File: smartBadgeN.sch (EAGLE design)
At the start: 62 parts, among them IC1 SI1304BDL, J1 10118192-0001LF, J2 LiPo, J3 505278-2433, Q1 MBT3904DW1T1, Q2 2.5A/30V, U1 CP2102N, U2 AP2112K-3.3V, U3 ESP-WROOM-32, U4 MCP73831

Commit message: revB init
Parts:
- C3: value 0.1uF -> 10uF
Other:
- note added: "Rev B"
- note removed: "Rev A"
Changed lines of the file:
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@@
 <parts>
 <part name="R9" library="resistor" library_urn="urn:adsk.eagle:library:348" deviceset="R-EU_" device="R0603" package3d_urn="urn:adsk.eagle:package:23555/3" value="1k"/>
-<part name="C3" library="resistor" library_urn="urn:adsk.eagle:library:348" deviceset="C-EU" device="C0603" package3d_urn="urn:adsk.eagle:package:23616/2" value="0.1uF"/>
+<part name="C3" library="resistor" library_urn="urn:adsk.eagle:library:348" deviceset="C-EU" device="C0603" package3d_urn="urn:adsk.eagle:package:23616/2" value="10uF"/>
 <part name="GND11" library="supply1" library_urn="urn:adsk.eagle:library:371" deviceset="GND" device=""/>
 <part name="C5" library="resistor" library_urn="urn:adsk.eagle:library:348" deviceset="C-EU" device="C1206" package3d_urn="urn:adsk.eagle:package:23618/2" value="100uF"/>
@@
 <text x="284.48" y="7.62" size="1.778" layer="94" align="bottom-right">Desgin by Moritz von Stietencron @ IoT-FabLab | www.iotfablab.eu | info@iotfablab.eu
 c/o BIBA - Bremer Institut für Produktion und Logistik GmbH | Hochschulring 20 | 28359 Bremen | GERMANY</text>
-<text x="378.46" y="7.62" size="1.778" layer="94" align="top-center">Rev A</text>
+<text x="378.46" y="7.62" size="1.778" layer="94" align="top-center">Rev B</text>
 <wire x1="289.56" y1="111.76" x2="289.56" y2="27.94" width="0.1524" layer="97"/>
 <text x="292.1" y="109.22" size="2.54" layer="97">Test Pads</text>

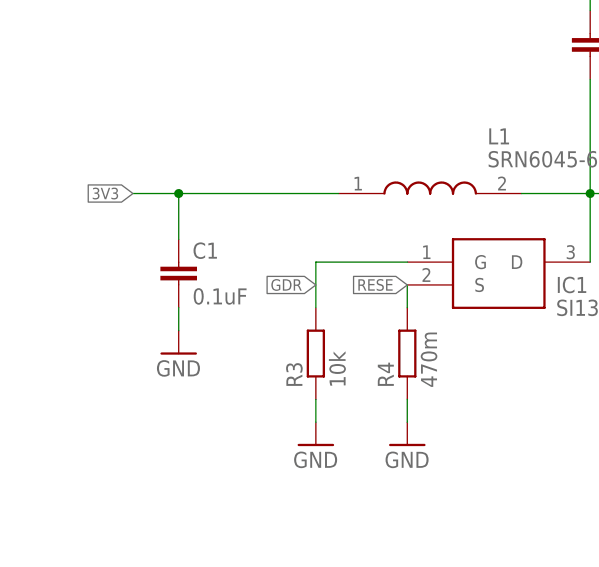
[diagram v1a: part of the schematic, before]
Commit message: capacitor values updated
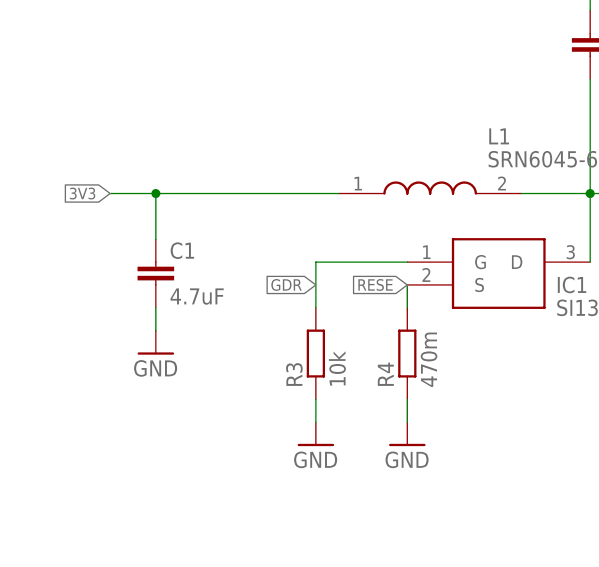
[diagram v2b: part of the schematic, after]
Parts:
- C1: value 0.1uF -> 4.7uF
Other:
- moved on the sheet: C1
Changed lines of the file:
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@@
 <part name="GND8" library="supply1" library_urn="urn:adsk.eagle:library:371" deviceset="GND" device=""/>
 <part name="L1" library="SamacSys_Parts" deviceset="SRN6045-680M" device=""/>
-<part name="C1" library="resistor" library_urn="urn:adsk.eagle:library:348" deviceset="C-EU" device="C0603" package3d_urn="urn:adsk.eagle:package:23616/2" value="0.1uF"/>
+<part name="C1" library="resistor" library_urn="urn:adsk.eagle:library:348" deviceset="C-EU" device="C0603" package3d_urn="urn:adsk.eagle:package:23616/2" value="4.7uF"/>
 <part name="IC1" library="SamacSys_Parts" deviceset="SI1304BDL-T1-E3" device="" value="SI1304BDL"/>
 <part name="R3" library="resistor" library_urn="urn:adsk.eagle:library:348" deviceset="R-EU_" device="R0603" package3d_urn="urn:adsk.eagle:package:23555/3" value="10k"/>
@@
 <attribute name="VALUE" x="57.15" y="80.01" size="1.778" layer="96" align="center-left"/>
 </instance>
-<instance part="C1" gate="G$1" x="22.86" y="68.58" smashed="yes">
-<attribute name="NAME" x="24.384" y="68.961" size="1.778" layer="95"/>
-<attribute name="VALUE" x="24.384" y="63.881" size="1.778" layer="96"/>
+<instance part="C1" gate="G$1" x="20.32" y="68.58" smashed="yes">
+<attribute name="NAME" x="21.844" y="68.961" size="1.778" layer="95"/>
+<attribute name="VALUE" x="21.844" y="63.881" size="1.778" layer="96"/>
 </instance>
 <instance part="IC1" gate="G$1" x="48.26" y="68.58" smashed="yes">
@@
 <attribute name="VALUE" x="81.28" y="132.08" size="1.778" layer="96"/>
 </instance>
-<instance part="GND1" gate="1" x="22.86" y="58.42" smashed="yes">
-<attribute name="VALUE" x="20.32" y="55.88" size="1.778" layer="96"/>
+<instance part="GND1" gate="1" x="20.32" y="58.42" smashed="yes">
+<attribute name="VALUE" x="17.78" y="55.88" size="1.778" layer="96"/>
 </instance>
 <instance part="GND4" gate="1" x="48.26" y="48.26" smashed="yes">
@@
 <pinref part="L1" gate="G$1" pin="1"/>
 <pinref part="C1" gate="G$1" pin="1"/>
-<wire x1="40.64" y1="76.2" x2="22.86" y2="76.2" width="0.1524" layer="91"/>
-<wire x1="22.86" y1="76.2" x2="22.86" y2="71.12" width="0.1524" layer="91"/>
-<wire x1="22.86" y1="76.2" x2="17.78" y2="76.2" width="0.1524" layer="91"/>
-<junction x="22.86" y="76.2"/>
-<label x="17.78" y="76.2" size="1.27" layer="95" rot="R180" xref="yes"/>
+<wire x1="40.64" y1="76.2" x2="20.32" y2="76.2" width="0.1524" layer="91"/>
+<wire x1="20.32" y1="76.2" x2="20.32" y2="71.12" width="0.1524" layer="91"/>
+<wire x1="20.32" y1="76.2" x2="15.24" y2="76.2" width="0.1524" layer="91"/>
+<junction x="20.32" y="76.2"/>
+<label x="15.24" y="76.2" size="1.27" layer="95" rot="R180" xref="yes"/>
 </segment>
 <segment>
@@
 <segment>
 <pinref part="C1" gate="G$1" pin="2"/>
-<wire x1="22.86" y1="63.5" x2="22.86" y2="60.96" width="0.1524" layer="91"/>
+<wire x1="20.32" y1="63.5" x2="20.32" y2="60.96" width="0.1524" layer="91"/>
 <pinref part="GND1" gate="1" pin="GND"/>
 </segment>

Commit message: schematics pdf added
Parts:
- removed J3: 505278-2433, SamacSys_Parts:505278-2433
- added EPD: MOLEX-FPC-CONN-24X0.5, BIBA:MOLEX-FPC-CONN-24X0.5
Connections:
- removed net N$15: C8.1, J3.5
- removed net N$16: C19.1, J3.4
- removed net N$24: C17.1, J3.18
- removed net N$25: C16.1, J3.20
- removed net N$26: C15.1, J3.22
- removed net N$27: C14.1, J3.24
- removed net N$33: C10.1, J3.19
- new net N$10: C16.1, EPD.P$20
- new net N$12: C15.1, EPD.P$22
- new net N$14: C14.1, EPD.P$24
- new net N$2: C17.1, EPD.P$18
- new net N$3: C10.1, EPD.P$19
- new net N$8: C19.1, EPD.P$4
- new net N$9: C8.1, EPD.P$5
- net 3V3: now also EPD.P$15, EPD.P$16; no longer J3.15, J3.16
- net BS: now also EPD.P$8; no longer J3.8
- net GDR: now also EPD.P$2; no longer J3.2
- net GND: now also EPD.P$17; no longer J3.17
- net IO13: now also EPD.P$13; no longer J3.13
- net IO14: now also EPD.P$14; no longer J3.14
- net IO15: now also EPD.P$12; no longer J3.12
- net IO25: now also EPD.P$9; no longer J3.9
- net IO26: now also EPD.P$10; no longer J3.10
- net IO27: now also EPD.P$11; no longer J3.11
- net N$18: now also D2.A; no longer D2.K
- net PREVGH: now also D2.K, EPD.P$21; no longer D2.A, J3.21
- net PREVGL: now also EPD.P$23; no longer J3.23
- net RESE: now also EPD.P$3; no longer J3.3
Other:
- moved on the sheet: C10, C11, C12, C14, C15, C16, C17, C19, C8, C9, D2, TP1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
